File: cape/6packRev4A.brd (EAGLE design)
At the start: 27.9 x 177.5 mm, 13 parts

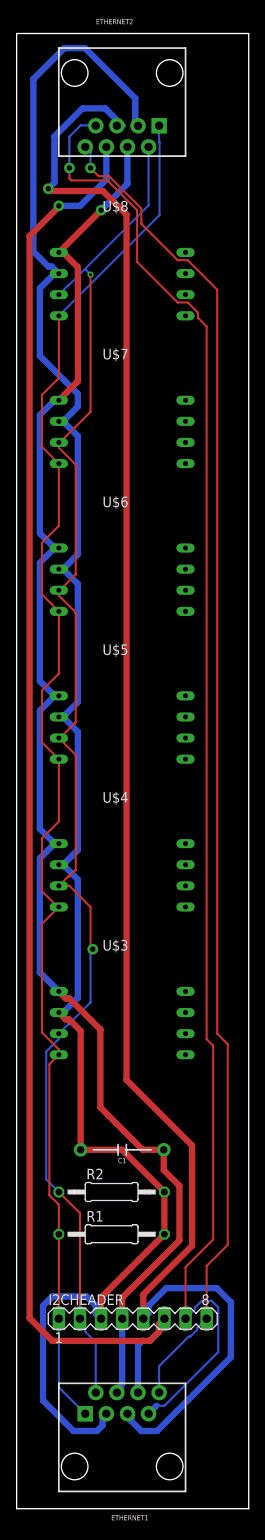
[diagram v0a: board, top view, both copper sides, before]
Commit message: Update cape/6packRev4A.brd
Fix minor issue with a via position and remove excess text.
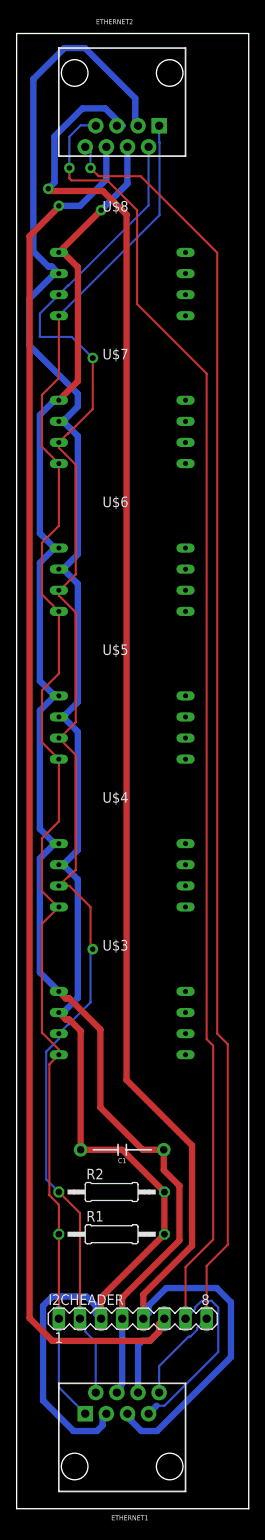
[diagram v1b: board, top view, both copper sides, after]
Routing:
- net SDA1: track 172.2 -> 174.7 mm
- net SCL2: track 161.9 -> 163.5 mm
- net +5V1: track 227.1 -> 228.2 mm
- net SDA2: track 179.8 -> 179.1 mm
